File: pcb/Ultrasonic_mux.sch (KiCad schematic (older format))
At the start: 71 parts, among them J0 DB9_Male, J2 DB9_Male, J3 DB9_Male, J4 DB9_Male, J5 DB9_Male, J8 DB9_Male, Q0 MMBT3904, Q2 MMBT3904, Q3 MMBT3904, Q4 MMBT3904, Q5 MMBT3904, Q8 MMBT3904, U1 FeatherM0

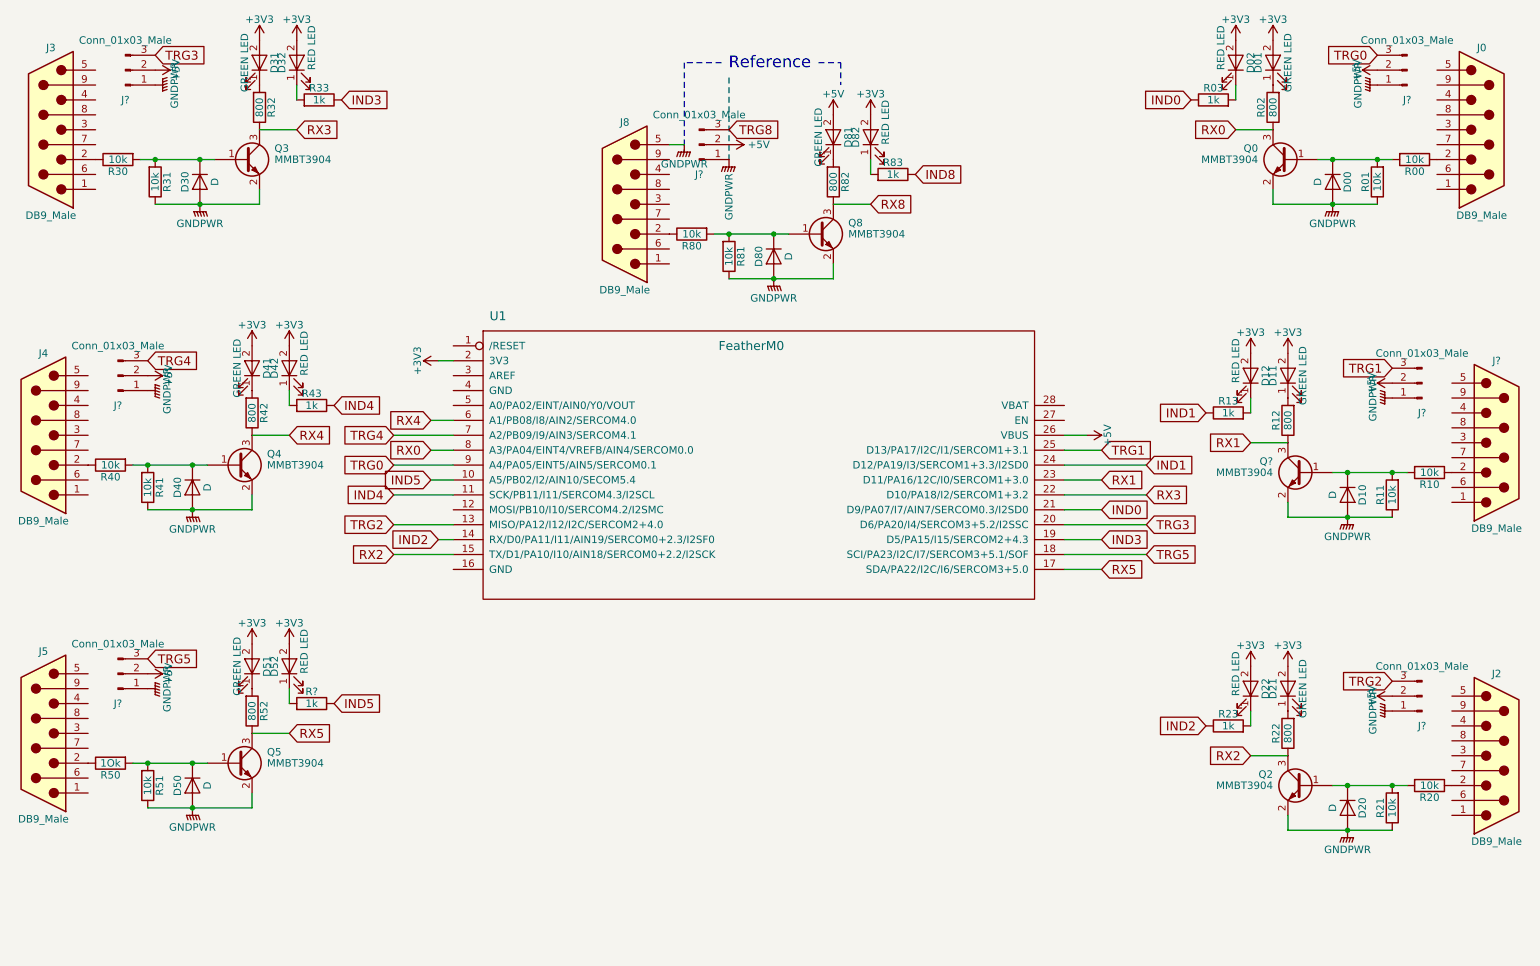
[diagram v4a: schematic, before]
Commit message: Changed voltage
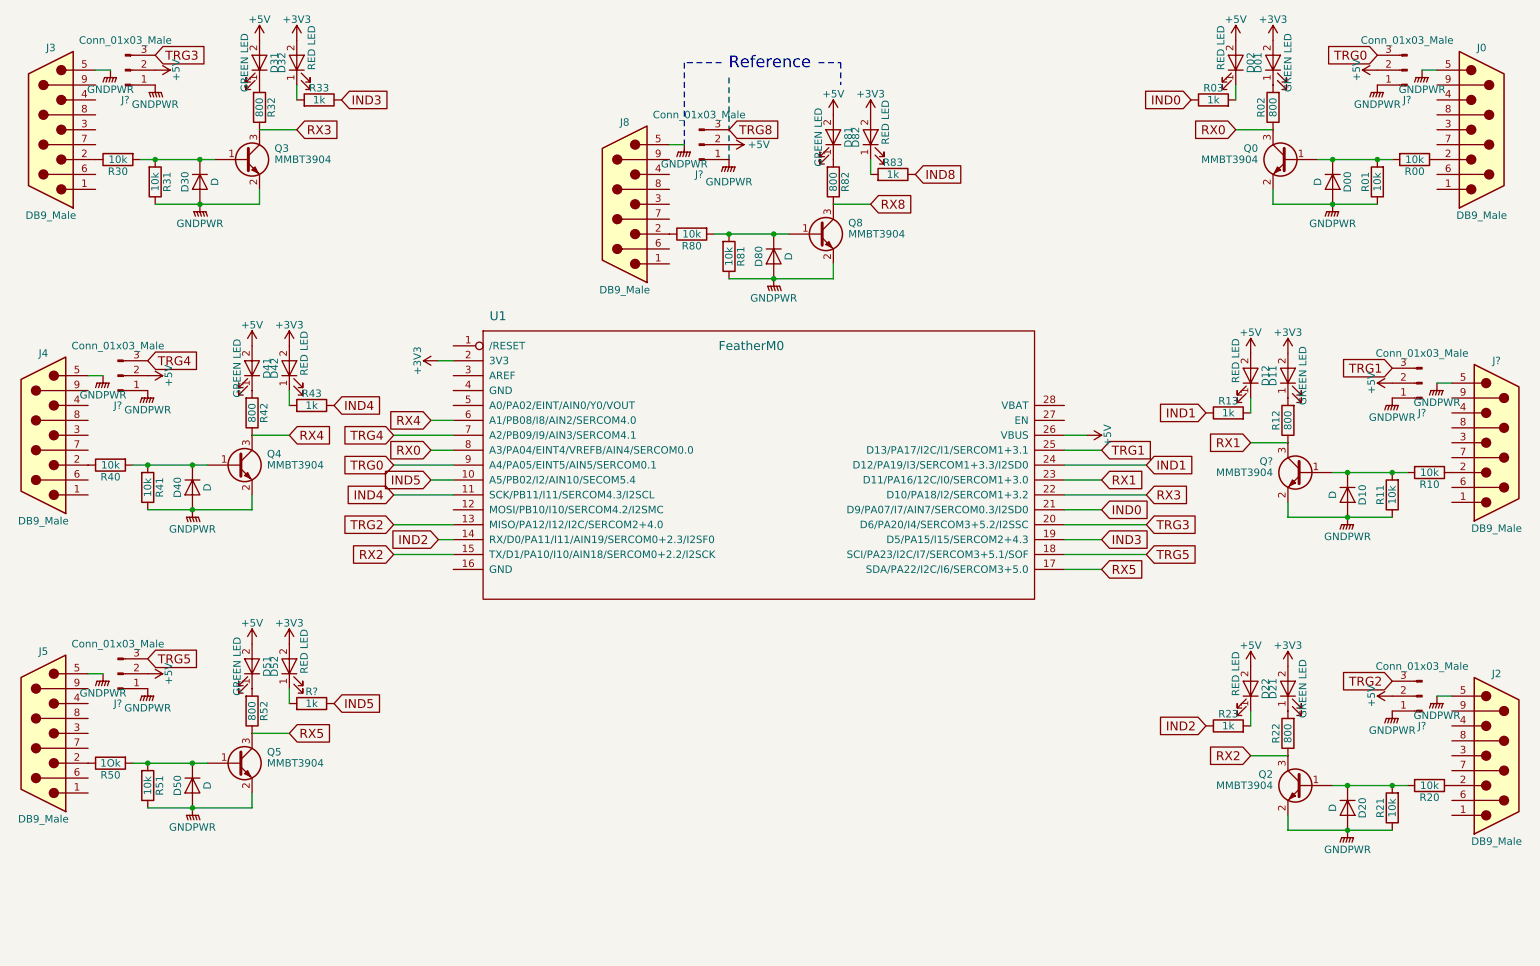
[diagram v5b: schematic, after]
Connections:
- net +3V3: no longer D02.2 (A), D12.2 (A), D22.2 (A), D31.2 (A), D41.2 (A), D51.2 (A)
- net +5V: now also D02.2 (A), D12.2 (A), D22.2 (A), D31.2 (A), D41.2 (A), D51.2 (A)
- net GNDPWR: now also J0.5, J2.5, J3.5, J4.5, J5.5, J?.5
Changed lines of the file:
@@
 	0    1    -1   0
-$EndComp
-$Comp
-L +3V3 #PWR?
-U 1 1 5A6FF886
-P 2400 750
-F 0 "#PWR?" H 2400 600 50  0001 C CNN
-F 1 "+3V3" H 2400 890 50  0000 C CNN
-F 2 "" H 2400 750 50  0001 C CNN
-F 3 "" H 2400 750 50  0001 C CNN
-	1    2400 750
-	-1   0    0    -1
 $EndComp
 Text GLabel 2650 1350 2    60   Input ~ 0
@@
 	0    1    -1   0
 $EndComp
-$Comp
-L +3V3 #PWR?
-U 1 1 5A704660
-P 2350 2800
-F 0 "#PWR?" H 2350 2650 50  0001 C CNN
-F 1 "+3V3" H 2350 2940 50  0000 C CNN
-F 2 "" H 2350 2800 50  0001 C CNN
-F 3 "" H 2350 2800 50  0001 C CNN
-	1    2350 2800
-	-1   0    0    -1
-$EndComp
 Text GLabel 2600 3400 2    60   Input ~ 0
 RX4
@@
 	0    1    -1   0
 $EndComp
-$Comp
-L +3V3 #PWR?
-U 1 1 5A70469E
-P 2350 4800
-F 0 "#PWR?" H 2350 4650 50  0001 C CNN
-F 1 "+3V3" H 2350 4940 50  0000 C CNN
-F 2 "" H 2350 4800 50  0001 C CNN
-F 3 "" H 2350 4800 50  0001 C CNN
-	1    2350 4800
-	-1   0    0    -1
-$EndComp
 Text GLabel 2600 5400 2    60   Input ~ 0
 RX5
@@
 F 3 "" H 9900 1000 50  0001 C CNN
 	1    9900 1050
-	0    1    1    0
+	1    0    0    -1
 $EndComp
 $Comp
@@
 F 3 "" H 10000 3100 50  0001 C CNN
 	1    10000 3150
-	0    1    1    0
+	1    0    0    -1
 $EndComp
 $Comp
@@
 F 3 "" H 1700 1000 50  0001 C CNN
 	1    1700 1050
-	0    -1   1    0
+	-1   0    0    -1
 $EndComp
 $Comp
@@
 F 3 "" H 10000 5200 50  0001 C CNN
 	1    10000 5250
-	0    1    1    0
+	1    0    0    -1
 $EndComp
 $Comp
@@
 F 3 "" H 1650 3050 50  0001 C CNN
 	1    1650 3100
-	0    -1   -1   0
+	1    0    0    -1
 $EndComp
 $Comp
@@
 F 3 "" H 1650 5050 50  0001 C CNN
 	1    1650 5100
-	0    -1   -1   0
+	1    0    0    -1
 $EndComp
 $Comp
@@
 P 5550 1550
 F 0 "#PWR?" H 5550 1350 50  0001 C CNN
-F 1 "GNDPWR" V 5550 1300 50  0000 C CNN
+F 1 "GNDPWR" H 5550 1400 50  0000 C CNN
 F 2 "" H 5550 1500 50  0001 C CNN
 F 3 "" H 5550 1500 50  0001 C CNN
@@
 $EndComp
 $Comp
-L +3V3 #PWR?
-U 1 1 5A73E3A9
-P 9050 2850
-F 0 "#PWR?" H 9050 2700 50  0001 C CNN
-F 1 "+3V3" H 9050 2990 50  0000 C CNN
-F 2 "" H 9050 2850 50  0001 C CNN
-F 3 "" H 9050 2850 50  0001 C CNN
-	1    9050 2850
-	-1   0    0    -1
-$EndComp
-$Comp
 L R R13
 U 1 1 5A73E3AF
@@
 $EndComp
 $Comp
-L +3V3 #PWR?
-U 1 1 5A742F77
-P 8950 750
-F 0 "#PWR?" H 8950 600 50  0001 C CNN
-F 1 "+3V3" H 8950 890 50  0000 C CNN
-F 2 "" H 8950 750 50  0001 C CNN
-F 3 "" H 8950 750 50  0001 C CNN
-	1    8950 750
-	-1   0    0    -1
-$EndComp
-$Comp
 L R R03
 U 1 1 5A742F7D
@@
 	1    9050 5100
 	0    1    -1   0
-$EndComp
-$Comp
-L +3V3 #PWR?
-U 1 1 5A74CE1A
-P 9050 4950
-F 0 "#PWR?" H 9050 4800 50  0001 C CNN
-F 1 "+3V3" H 9050 5090 50  0000 C CNN
-F 2 "" H 9050 4950 50  0001 C CNN
-F 3 "" H 9050 4950 50  0001 C CNN
-	1    9050 4950
-	-1   0    0    -1
 $EndComp
 $Comp
@@
 Wire Wire Line
 	5150 1450 5250 1450
+$Comp
+L +5V #PWR?
+U 1 1 5A74F00A
+P 8950 750
+F 0 "#PWR?" H 8950 600 50  0001 C CNN
+F 1 "+5V" H 8950 890 50  0000 C CNN
+F 2 "" H 8950 750 50  0001 C CNN
+F 3 "" H 8950 750 50  0001 C CNN
+	1    8950 750
+	1    0    0    -1
+$EndComp
+$Comp
+L +5V #PWR?
+U 1 1 5A74F873
+P 9050 2850
+F 0 "#PWR?" H 9050 2700 50  0001 C CNN
+F 1 "+5V" H 9050 2990 50  0000 C CNN
+F 2 "" H 9050 2850 50  0001 C CNN
+F 3 "" H 9050 2850 50  0001 C CNN
+	1    9050 2850
+	1    0    0    -1
+$EndComp
+$Comp
+L +5V #PWR?
+U 1 1 5A74F95F
+P 9050 4950
+F 0 "#PWR?" H 9050 4800 50  0001 C CNN
+F 1 "+5V" H 9050 5090 50  0000 C CNN
+F 2 "" H 9050 4950 50  0001 C CNN
+F 3 "" H 9050 4950 50  0001 C CNN
+	1    9050 4950
+	1    0    0    -1
+$EndComp
+$Comp
+L +5V #PWR?
+U 1 1 5A74FA4B
+P 2350 4800
+F 0 "#PWR?" H 2350 4650 50  0001 C CNN
+F 1 "+5V" H 2350 4940 50  0000 C CNN
+F 2 "" H 2350 4800 50  0001 C CNN
+F 3 "" H 2350 4800 50  0001 C CNN
+	1    2350 4800
+	1    0    0    -1
+$EndComp
+$Comp
+L +5V #PWR?
+U 1 1 5A74FB37
+P 2350 2800
+F 0 "#PWR?" H 2350 2650 50  0001 C CNN
+F 1 "+5V" H 2350 2940 50  0000 C CNN
+F 2 "" H 2350 2800 50  0001 C CNN
+F 3 "" H 2350 2800 50  0001 C CNN
+	1    2350 2800
+	1    0    0    -1
+$EndComp
+$Comp
+L +5V #PWR?
+U 1 1 5A74FCF8
+P 2400 750
+F 0 "#PWR?" H 2400 600 50  0001 C CNN
+F 1 "+5V" H 2400 890 50  0000 C CNN
+F 2 "" H 2400 750 50  0001 C CNN
+F 3 "" H 2400 750 50  0001 C CNN
+	1    2400 750
+	1    0    0    -1
+$EndComp
+$Comp
+L GNDPWR #PWR?
+U 1 1 5A753ECC
+P 1400 950
+F 0 "#PWR?" H 1400 750 50  0001 C CNN
+F 1 "GNDPWR" H 1400 820 50  0000 C CNN
+F 2 "" H 1400 900 50  0001 C CNN
+F 3 "" H 1400 900 50  0001 C CNN
+	1    1400 950
+	1    0    0    -1
+$EndComp
+Wire Wire Line
+	1300 950  1400 950
+$Comp
+L GNDPWR #PWR?
+U 1 1 5A75476E
+P 1350 3000
+F 0 "#PWR?" H 1350 2800 50  0001 C CNN
+F 1 "GNDPWR" H 1350 2870 50  0000 C CNN
+F 2 "" H 1350 2950 50  0001 C CNN
+F 3 "" H 1350 2950 50  0001 C CNN
+	1    1350 3000
+	1    0    0    -1
+$EndComp
+Wire Wire Line
+	1250 3000 1350 3000
+$Comp
+L GNDPWR #PWR?
+U 1 1 5A75562A
+P 1350 5000
+F 0 "#PWR?" H 1350 4800 50  0001 C CNN
+F 1 "GNDPWR" H 1350 4870 50  0000 C CNN
+F 2 "" H 1350 4950 50  0001 C CNN
+F 3 "" H 1350 4950 50  0001 C CNN
+	1    1350 5000
+	1    0    0    -1
+$EndComp
+Wire Wire Line
+	1250 5000 1350 5000
+$Comp
+L GNDPWR #PWR?
+U 1 1 5A757429
+P 10300 5150
+F 0 "#PWR?" H 10300 4950 50  0001 C CNN
+F 1 "GNDPWR" H 10300 5020 50  0000 C CNN
+F 2 "" H 10300 5100 50  0001 C CNN
+F 3 "" H 10300 5100 50  0001 C CNN
+	1    10300 5150
+	1    0    0    -1
+$EndComp
+Wire Wire Line
+	10400 5150 10300 5150
+$Comp
+L GNDPWR #PWR?
+U 1 1 5A7585CC
+P 10300 3050
+F 0 "#PWR?" H 10300 2850 50  0001 C CNN
+F 1 "GNDPWR" H 10300 2920 50  0000 C CNN
+F 2 "" H 10300 3000 50  0001 C CNN
+F 3 "" H 10300 3000 50  0001 C CNN
+	1    10300 3050
+	1    0    0    -1
+$EndComp
+Wire Wire Line
+	10400 3050 10300 3050
+$Comp
+L GNDPWR #PWR?
+U 1 1 5A758BA8
+P 10200 950
+F 0 "#PWR?" H 10200 750 50  0001 C CNN
+F 1 "GNDPWR" H 10200 820 50  0000 C CNN
+F 2 "" H 10200 900 50  0001 C CNN
+F 3 "" H 10200 900 50  0001 C CNN
+	1    10200 950
+	1    0    0    -1
+$EndComp
+Wire Wire Line
+	10300 950  10200 950
 $EndSCHEMATC

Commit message: Finished schematic
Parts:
- removed D80: D, symbol D
- removed D81: GREEN LED, symbol LED
- removed D82: RED LED, symbol LED
- removed J8: DB9_Male, symbol DB9_Male
- removed J?: Conn_01x03_Male, symbol Conn_01x03_Male
- removed Q8: MMBT3904, TO_SOT_Packages_SMD:SOT-23, symbol MMBT3904
- removed R80, R81: 10k, symbol R
- removed R82: 800, symbol R
- removed R83: 1k, symbol R
- added +3V3, +5V, GND, P1, P12, P27, P28, P3, P5: (no value), symbol Conn_01x01
- R02, R12, R22, R32, R42, R52: value 800 -> 1k
- gave numbers to parts that had none: 9
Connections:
- net +3V3: now also +3V3.1 (Pin_1)
- net +5V: now also +5V.1 (Pin_1)
- net GNDPWR: now also U1.16 (GND), U1.4 (GND), GND.1 (Pin_1)
- net RX2: now also U1.13 (MISO/PA12/I12/I2C/SERCOM2+4.0); no longer U1.15 (TX/D1/PA10/I10/AIN18/SERCOM0+2.2/I2SCK)
- net TRG2: now also U1.15 (TX/D1/PA10/I10/AIN18/SERCOM0+2.2/I2SCK); no longer U1.13 (MISO/PA12/I12/I2C/SERCOM2+4.0)
- net at U1.1 (/RESET): now also P1.1 (Pin_1)
- net at U1.12 (MOSI/PB10/I10/SERCOM4.2/I2SMC): now also P12.1 (Pin_1)
- net at U1.27 (EN): now also P27.1 (Pin_1)
- net at U1.28 (VBAT): now also P28.1 (Pin_1)
- net at U1.3 (AREF): now also P3.1 (Pin_1)
- net at U1.5 (A0/PA02/EINT/AIN0/Y0/VOUT): now also P5.1 (Pin_1)
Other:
- note removed: "Reference"
- moved on the sheet: D00, D01, D02, D10, D11, D12, D20, D21, D22, D30, D31, D32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

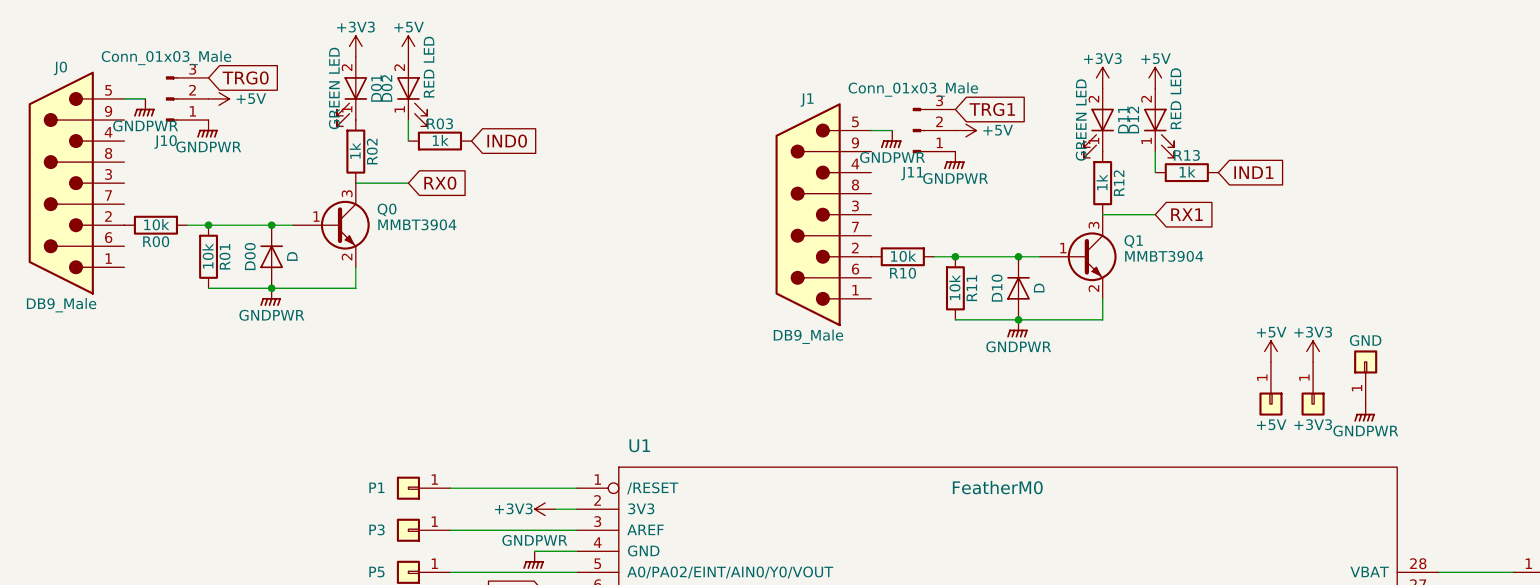
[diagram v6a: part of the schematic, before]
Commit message: Added netlist restarted footprint associations for board
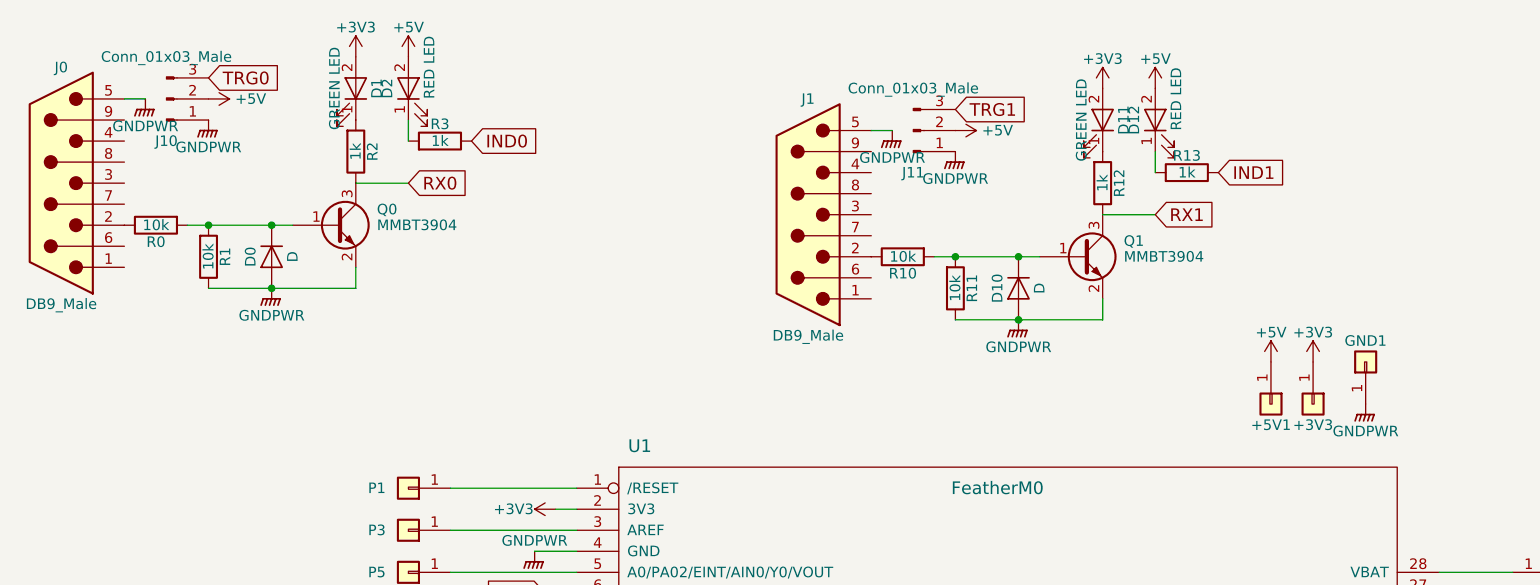
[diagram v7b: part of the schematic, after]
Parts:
- D1: renamed from D01; footprint (none) -> LEDs:LED_0805_HandSoldering
- D11, D21, D31, D41, D51: footprint (none) -> LEDs:LED_0805_HandSoldering
- D12, D22, D32, D42, D52: footprint (none) -> LEDs:LED_0603_HandSoldering
- D2: renamed from D02; footprint (none) -> LEDs:LED_0603_HandSoldering
- renumbered +5V to +5V1, D00 to D0, GND to GND1, R00 to R0, R01 to R1, R02 to R2, R03 to R3
